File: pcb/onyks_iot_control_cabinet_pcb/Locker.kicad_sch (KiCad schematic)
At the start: 12 parts, among them J6 Screw_Terminal_01x02, J7 Conn_01x02_Socket, Q3 PMV100ENEAR, Q4 PMV100ENEAR, SW3 SW_Push

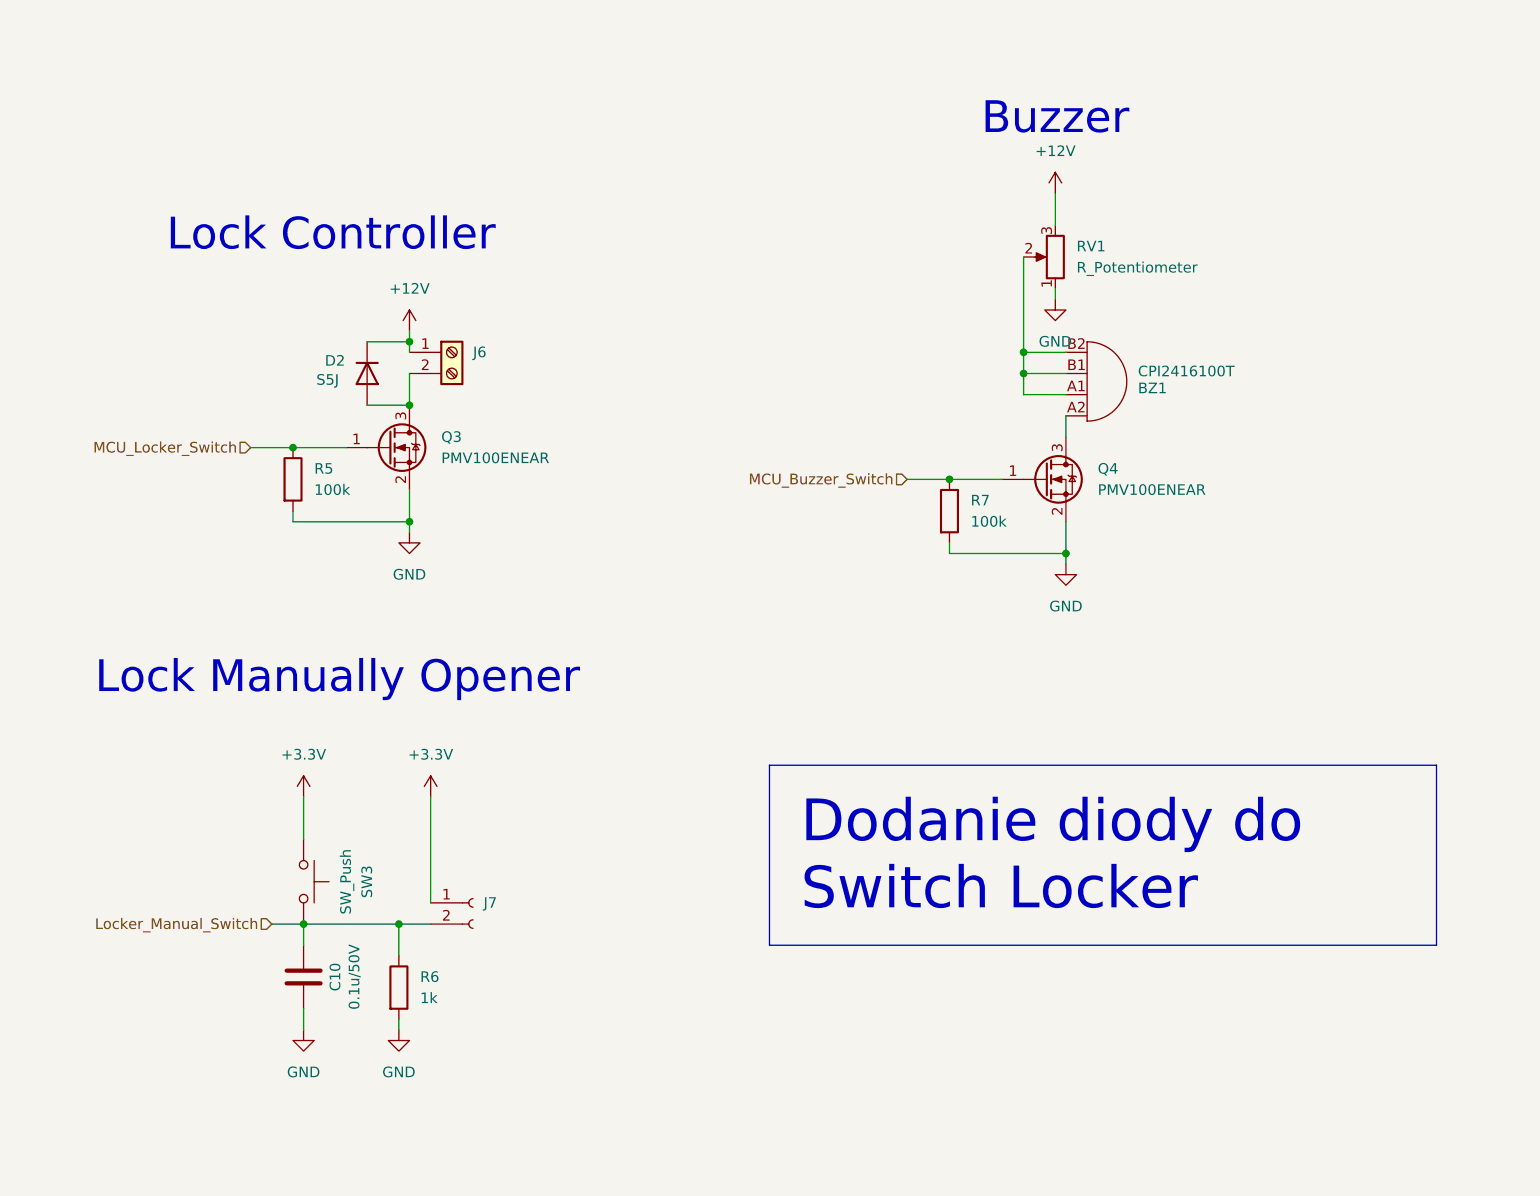
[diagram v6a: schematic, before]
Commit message: Update of the power supply and added the header for 125kHz RFID
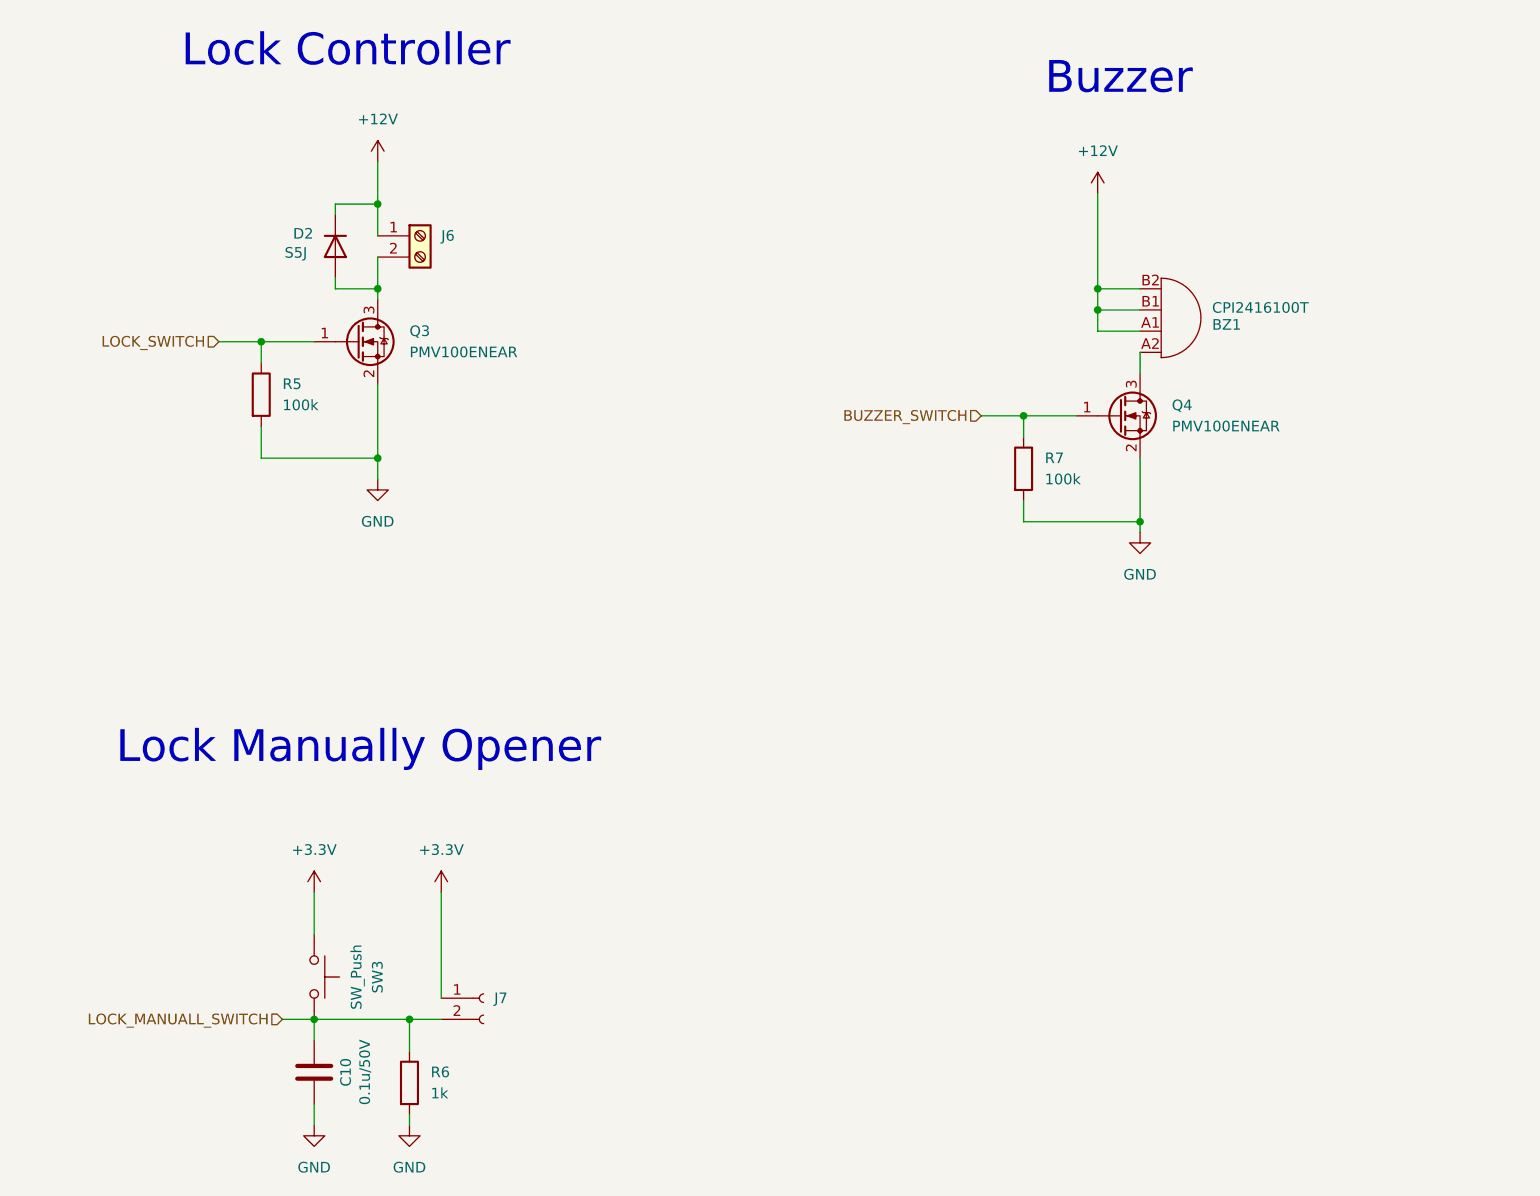
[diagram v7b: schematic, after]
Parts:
- removed RV1: R_Potentiometer, Potentiometer_THT:Potentiometer_Vishay_T73YP_Vertical, symbol Device:R_Potentiometer
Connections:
- net +12V: now also BZ1.A1 (-_1), BZ1.B1 (+_1), BZ1.B2 (+_2)
- net Locker_Manual_Switch renamed LOCK_MANUALL_SWITCH
- net MCU_Buzzer_Switch renamed BUZZER_SWITCH
- net MCU_Locker_Switch renamed LOCK_SWITCH
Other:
- company: (none) -> ,,Onyks'' Students Scientific Association
- title: (none) -> Onyks Iot Control Cabinet
- moved on the sheet: BZ1, C10, D2, J6, J7, Q3, Q4, R5, R6, R7, SW3

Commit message: Schematics update; power supply and footprints fixes
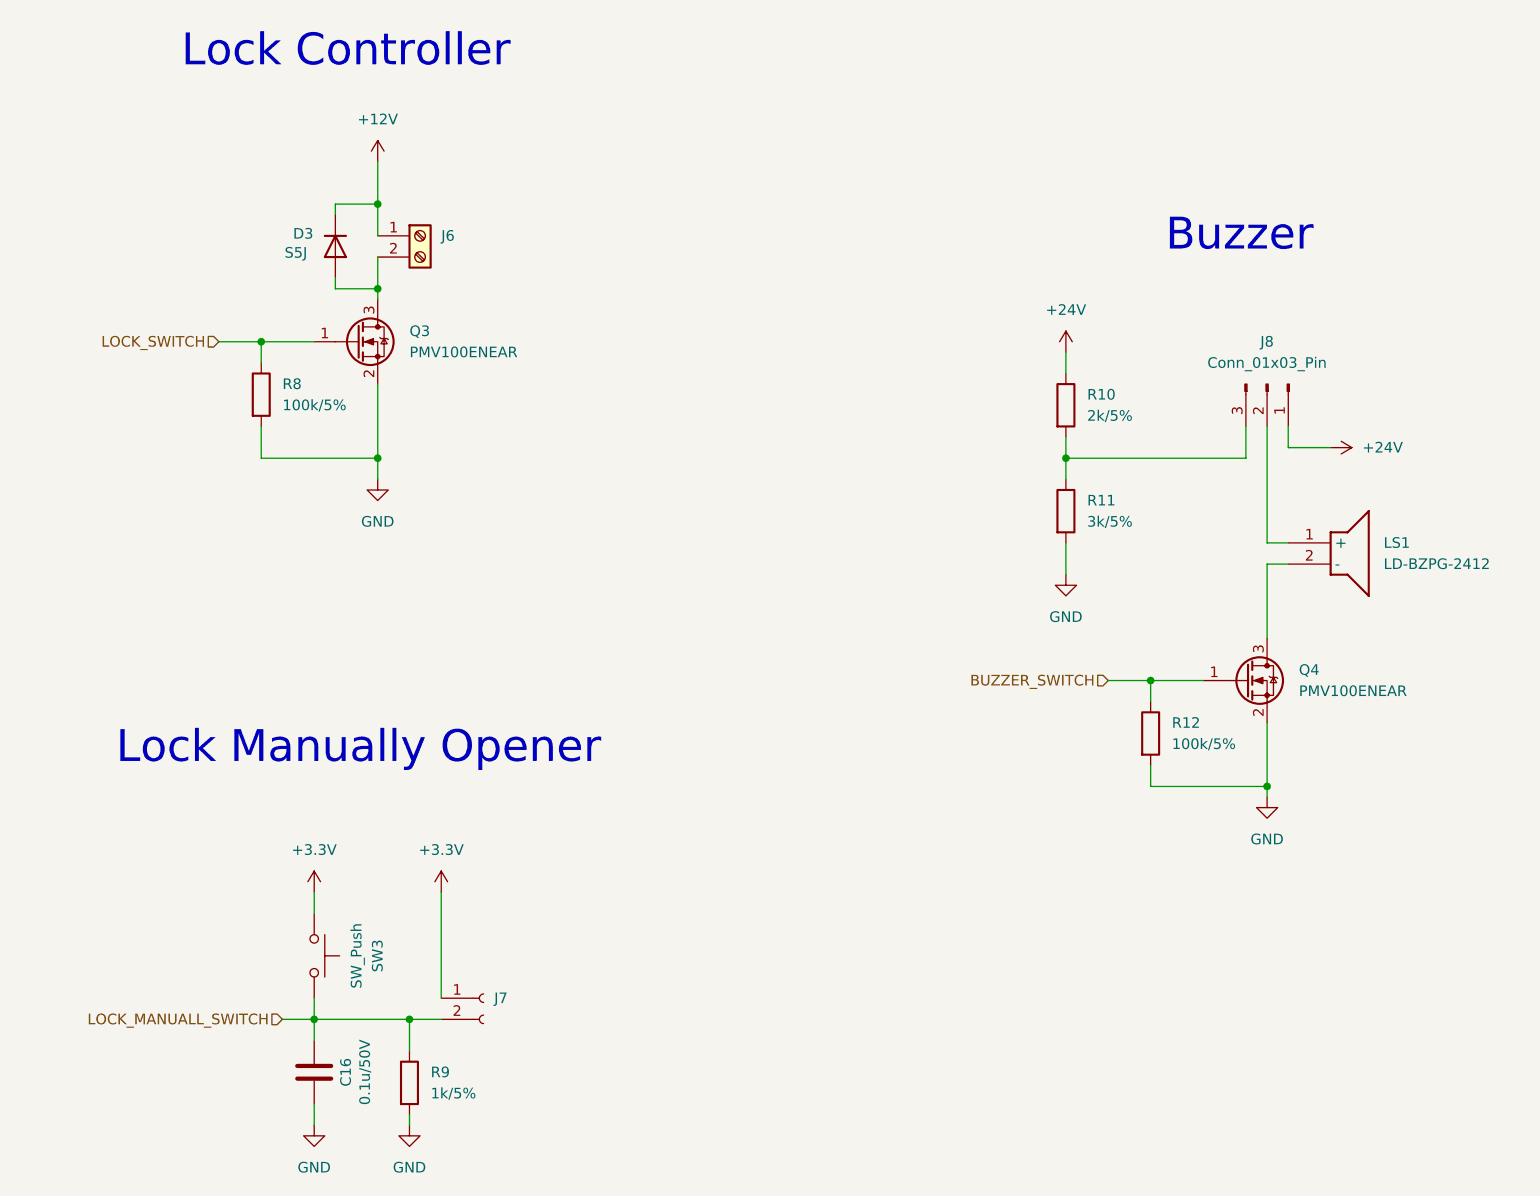
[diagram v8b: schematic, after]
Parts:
- removed BZ1: CPI2416100T, ourFootprints:CPI2416100T, symbol Device:Buzzer
- added J8: Conn_01x03_Pin, Connector_PinHeader_2.54mm:PinHeader_1x03_P2.54mm_Vertical, symbol Connector:Conn_01x03_Pin
- added LS1: LD-BZPG-2412, footprints:LDBZPG2412, symbol LD-BZPG-2412:LD-BZPG-2412
- added R10: 2k/5%, Resistor_SMD:R_0805_2012Metric_Pad1.20x1.40mm_HandSolder, symbol Device:R
- added R11: 3k/5%, Resistor_SMD:R_0805_2012Metric_Pad1.20x1.40mm_HandSolder, symbol Device:R
- J6: footprint TerminalBlock:TerminalBlock_Xinya_XY308-2.54-2P_1x02_P2.54mm_Horizontal -> TerminalBlock:TerminalBlock_Altech_AK300-2_P5.00mm
- R12: renamed from R7; value 100k -> 100k/5%
- R8: renamed from R5; value 100k -> 100k/5%
- R9: renamed from R6; value 1k -> 1k/5%
- renumbered C10 to C16, D2 to D3
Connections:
- net GND: now also R11.2
- net at Q4.3 (D): now also LS1.2 (-)
- new net: J8.3 (Pin_3), R10.2, R11.1
- new net: J8.2 (Pin_2), LS1.1 (+)
- new net +24V: J8.1 (Pin_1), R10.1
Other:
- moved on the sheet: Q4, R12, SW3
